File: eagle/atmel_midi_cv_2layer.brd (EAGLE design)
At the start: 98.7 x 49.5 mm, 52 parts, among them IC2 TL072P, Q1 16M, U1 ATMEGA328P_PDIP, U2 TLV2372IP

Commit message: started software update
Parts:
- moved TONE 12.7 mm to (53.3, 0.00)
- moved VEL 12.7 mm to (66.0, 0.00)
- moved R4 10.2 mm to (44.5, 19.1)
- moved R15 2.84 mm to (44.5, 21.6)
- renumbered CV_BUS_ENABLE to BUS_CV, GATE_BUS_ENABLE to BUS_GATE
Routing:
- net N$39: track 44.9 -> 111.2 mm, vias 2 -> 0
- net +12V: track 120.2 -> 58.4 mm, vias 2 -> 0
- net N$35: track 69.7 -> 37.1 mm
- net N$19: track 0.00 -> 15.2 mm
- net +5V: track 138.6 -> 148.7 mm, vias 1 -> 0
- net N$15: track 68.9 -> 78.7 mm, vias 1 -> 0
- net N$30: track 56.7 -> 64.5 mm
- net N$9: track 3.57 -> 7.79 mm
- net N$38: track 20.4 -> 16.8 mm
- net N$31: track 7.00 -> 10.5 mm
- net N$24: track 0.00 -> 3.38 mm
- net N$22: track 27.4 -> 28.5 mm, vias 0 -> 1
- net N$23: track 9.04 -> 7.93 mm
- net N$28: track 73.9 -> 72.8 mm
- net N$16: track 20.5 -> 19.7 mm
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
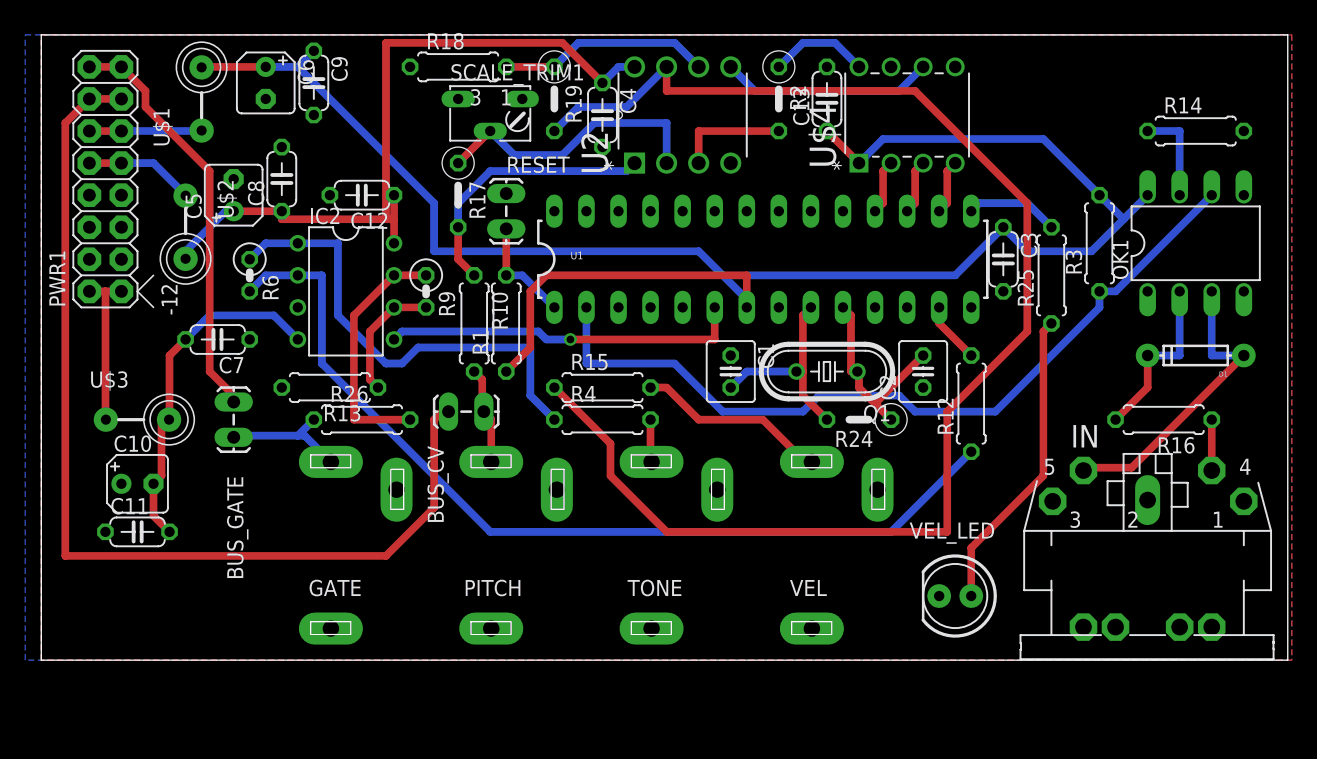
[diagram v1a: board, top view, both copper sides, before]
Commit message: added url and release to silkscreen
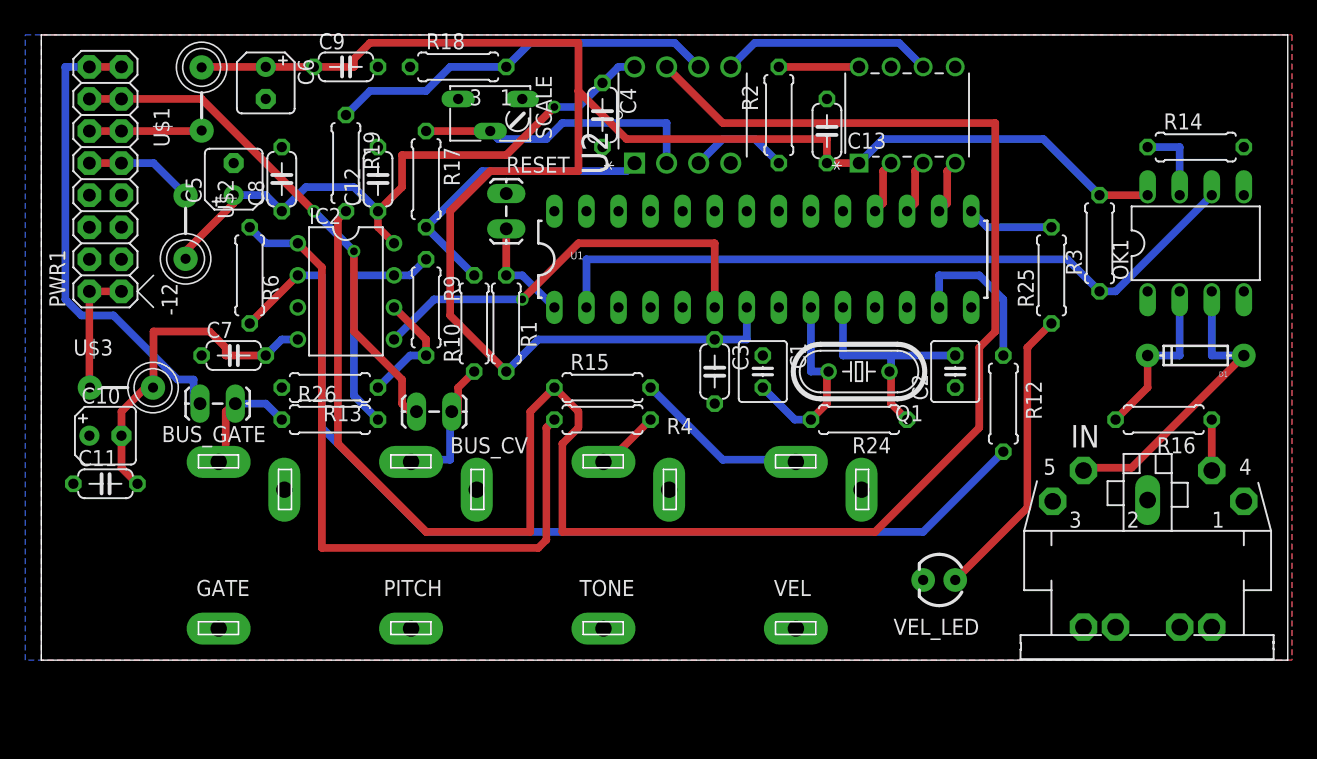
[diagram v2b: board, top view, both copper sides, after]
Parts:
- R17, R19, R2, R24: device rcl:0207/5V -> rcl:0207/7
- R6, R9: device rcl:0207/2V -> rcl:0207/7
- VEL_LED: device SparkFun-LED:LED5MM -> SparkFun-LED:LED3MM
- moved C3 24.5 mm to (53.3, 22.9)
- moved R19 17.3 mm to (24.1, 39.4)
- moved GATE 8.89 mm to (19.1, 0.00)
- moved PITCH 6.35 mm to (34.3, 0.00)
- moved C10 4.58 mm to (5.08, 17.8)
- moved C11 4.58 mm to (5.08, 14.0)
- moved TONE 3.81 mm to (49.5, 0.00)
- moved R17 2.84 mm to (30.5, 38.1)
- moved C9 2.84 mm to (24.1, 47.0), turned to 0 degrees
- moved U$3 2.84 mm to (6.35, 21.6)
- moved C13 2.54 mm to (62.2, 41.9)
- moved C2 2.54 mm to (72.4, 22.9)
- moved R12 2.54 mm to (76.2, 20.3)
- moved BUS_CV 2.54 mm to (29.8, 19.7)
- moved BUS_GATE 2.54 mm to (15.2, 20.3), turned to 180 degrees
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- renumbered SCALE_TRIM1 to SCALE
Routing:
- net N$39: track 111.2 -> 150.7 mm
- net N$15: track 78.7 -> 41.0 mm, vias 0 -> 2
- net N$35: track 37.1 -> 57.1 mm
- net N$38: track 16.8 -> 31.1 mm
- net +12V: track 58.4 -> 49.8 mm, vias 0 -> 1
- net N$21: track 4.86 -> 12.9 mm
- net +5V: track 148.7 -> 141.1 mm
- net N$30: track 64.5 -> 57.5 mm
- net N$28: track 72.8 -> 79.4 mm
- net N$1: track 32.8 -> 38.1 mm
- net N$22: track 28.5 -> 33.6 mm
- net N$9: track 7.79 -> 11.3 mm
- net N$17: track 12.7 -> 10.2 mm
- net N$41: track 21.5 -> 24.0 mm
- net N$5: track 16.2 -> 18.6 mm
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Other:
- board text added: "Release v0.5"
- board text added: "https://github.com/jbeuckm/atmega_midi_cv_basic"
